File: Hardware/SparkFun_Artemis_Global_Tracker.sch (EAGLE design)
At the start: 139 parts, among them J1 IRIDIUM_9603N, J2 USB-C, J6 U.FL, J7 ANTENNA-GROUNDEDEDGE_SMA, J8 STANDOFFS_M2X0.4_STEEL_6MM, J9 STANDOFFS_M2X0.4_STEEL_6MM, Q1 5.8A/30V/35mΩ, Q2 20V/4.2A/52mΩ/1.4W, Q3 20V/4.2A/52mΩ/1.4W, Q4 600mA/40V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

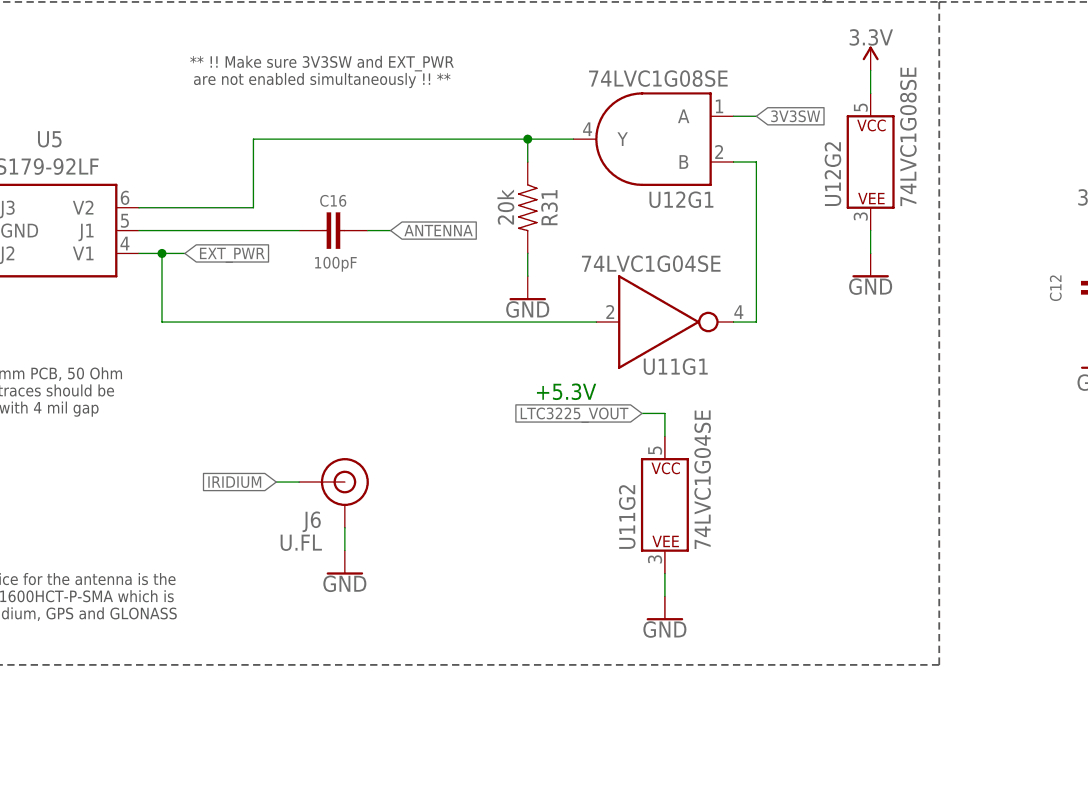
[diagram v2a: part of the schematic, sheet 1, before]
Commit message: powering U11 from 3.3V
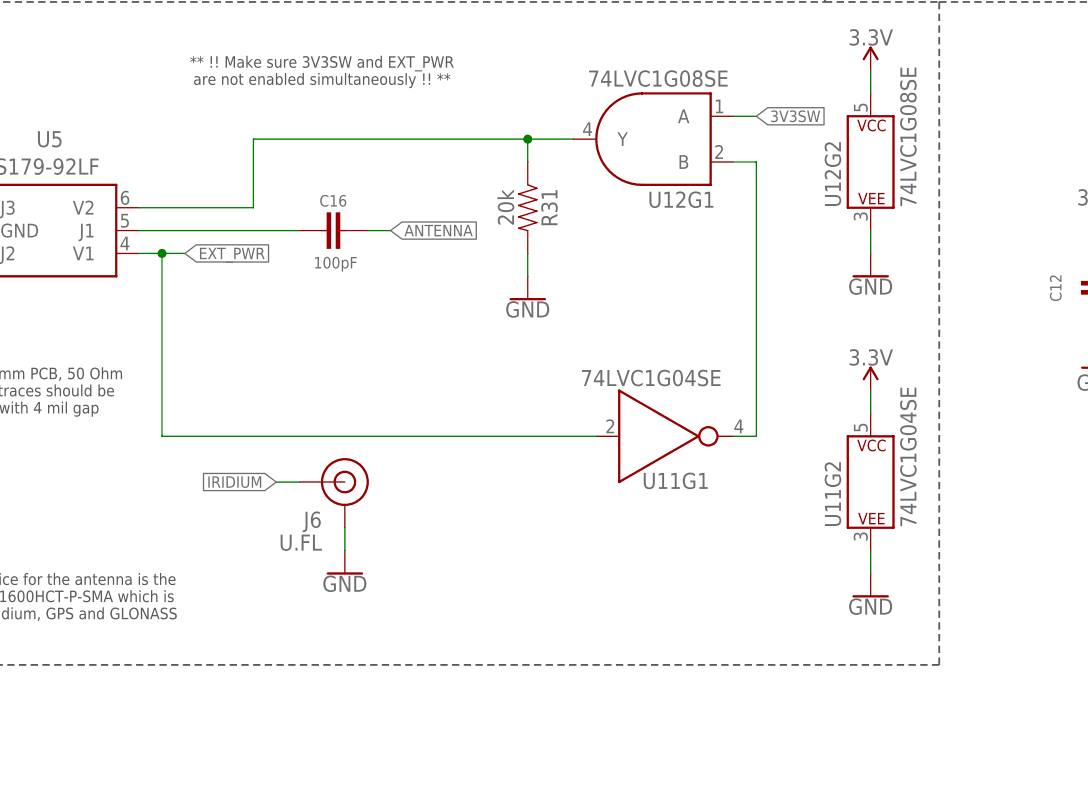
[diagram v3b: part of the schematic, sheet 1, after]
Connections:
- net 3.3V: now also U11G2.P$V+
- net LTC3225_VOUT: no longer U11G2.P$V+
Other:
- moved on the sheet: U11G1, U11G2
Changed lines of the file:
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@@
 <part name="SUPPLY3" library="SparkFun-PowerSymbols" deviceset="3.3V" device=""/>
 <part name="GND3" library="SparkFun-PowerSymbols" deviceset="GND" device=""/>
+<part name="SUPPLY19" library="SparkFun-PowerSymbols" deviceset="3.3V" device=""/>
 </parts>
 <sheets>
@@
 antenna traces should be
 32 mil with 4 mil gap </text>
-<text x="266.7" y="150.622" size="1.778" layer="91" font="vector" rot="R180">+5.3V</text>
 <wire x1="304.8" y1="193.04" x2="304.8" y2="119.38" width="0.2032" layer="97" style="longdash"/>
 <wire x1="304.8" y1="119.38" x2="162.56" y2="119.38" width="0.2032" layer="97" style="longdash"/>
@@
 <attribute name="VALUE" x="236.22" y="132.08" size="1.778" layer="96" font="vector" rot="MR0"/>
 </instance>
-<instance part="GND40" gate="1" x="274.32" y="124.46" smashed="yes">
-<attribute name="VALUE" x="274.32" y="124.206" size="1.778" layer="96" font="vector" align="top-center"/>
+<instance part="GND40" gate="1" x="297.18" y="127" smashed="yes">
+<attribute name="VALUE" x="297.18" y="126.746" size="1.778" layer="96" font="vector" align="top-center"/>
 </instance>
 <instance part="GND44" gate="1" x="297.18" y="162.56" smashed="yes">
@@
 <attribute name="VALUE" x="302.26" y="170.18" size="1.778" layer="95" font="vector" rot="R90"/>
 </instance>
-<instance part="U11" gate="G1" x="271.78" y="157.48" smashed="yes">
-<attribute name="NAME" x="271.78" y="151.638" size="1.778" layer="95" font="vector"/>
-<attribute name="VALUE" x="264.922" y="163.068" size="1.778" layer="95" font="vector"/>
-</instance>
-<instance part="U11" gate="G2" x="274.32" y="137.16" smashed="yes">
-<attribute name="NAME" x="271.018" y="132.08" size="1.778" layer="95" font="vector" rot="R90"/>
-<attribute name="VALUE" x="279.4" y="132.08" size="1.778" layer="95" font="vector" rot="R90"/>
+<instance part="U11" gate="G1" x="271.78" y="144.78" smashed="yes">
+<attribute name="NAME" x="271.78" y="138.938" size="1.778" layer="95" font="vector"/>
+<attribute name="VALUE" x="264.922" y="150.368" size="1.778" layer="95" font="vector"/>
+</instance>
+<instance part="U11" gate="G2" x="297.18" y="139.7" smashed="yes">
+<attribute name="NAME" x="293.878" y="134.62" size="1.778" layer="95" font="vector" rot="R90"/>
+<attribute name="VALUE" x="302.26" y="134.62" size="1.778" layer="95" font="vector" rot="R90"/>
 </instance>
 <instance part="R31" gate="G$1" x="259.08" y="170.18" smashed="yes" rot="R270">
@@
 <instance part="GND3" gate="1" x="322.58" y="152.4" smashed="yes">
 <attribute name="VALUE" x="320.04" y="149.86" size="1.778" layer="96" font="vector"/>
+</instance>
+<instance part="SUPPLY19" gate="G$1" x="297.18" y="149.86" smashed="yes">
+<attribute name="VALUE" x="297.18" y="152.654" size="1.778" layer="96" font="vector" align="bottom-center"/>
 </instance>
 </instances>
@@
 <pinref part="SUPPLY13" gate="G$1" pin="3.3V"/>
 <wire x1="332.74" y1="167.64" x2="332.74" y2="165.1" width="0.1524" layer="91"/>
+</segment>
+<segment>
+<pinref part="SUPPLY19" gate="G$1" pin="3.3V"/>
+<wire x1="297.18" y1="149.86" x2="297.18" y2="147.32" width="0.1524" layer="91"/>
+<pinref part="U11" gate="G2" pin="P$V+"/>
 </segment>
 </net>
@@
 </segment>
 <segment>
-<wire x1="274.32" y1="129.54" x2="274.32" y2="127" width="0.1524" layer="91"/>
+<wire x1="297.18" y1="132.08" x2="297.18" y2="129.54" width="0.1524" layer="91"/>
 <pinref part="GND40" gate="1" pin="GND"/>
 <pinref part="U11" gate="G2" pin="P$V-"/>
@@
 <wire x1="215.9" y1="165.1" x2="218.44" y2="165.1" width="0.1524" layer="91"/>
 <wire x1="218.44" y1="165.1" x2="220.98" y2="165.1" width="0.1524" layer="91"/>
-<wire x1="218.44" y1="165.1" x2="218.44" y2="157.48" width="0.1524" layer="91"/>
+<wire x1="218.44" y1="165.1" x2="218.44" y2="144.78" width="0.1524" layer="91"/>
 <junction x="218.44" y="165.1"/>
-<wire x1="218.44" y1="157.48" x2="266.7" y2="157.48" width="0.1524" layer="91"/>
+<wire x1="218.44" y1="144.78" x2="266.7" y2="144.78" width="0.1524" layer="91"/>
 <pinref part="U11" gate="G1" pin="A"/>
 </segment>
@@
 <label x="83.82" y="266.7" size="1.27" layer="95" font="vector" xref="yes"/>
 </segment>
-<segment>
-<wire x1="274.32" y1="147.32" x2="271.78" y2="147.32" width="0.1524" layer="91"/>
-<label x="271.78" y="147.32" size="1.27" layer="95" font="vector" rot="R180" xref="yes"/>
-<wire x1="274.32" y1="144.78" x2="274.32" y2="147.32" width="0.1524" layer="91"/>
-<pinref part="U11" gate="G2" pin="P$V+"/>
-</segment>
 </net>
 <net name="ARTEMIS_D28" class="0">
@@
 <net name="N$33" class="0">
 <segment>
-<wire x1="284.48" y1="157.48" x2="284.48" y2="175.26" width="0.1524" layer="91"/>
+<wire x1="284.48" y1="144.78" x2="284.48" y2="175.26" width="0.1524" layer="91"/>
 <wire x1="284.48" y1="175.26" x2="281.94" y2="175.26" width="0.1524" layer="91"/>
 <pinref part="U12" gate="G1" pin="B"/>
 <pinref part="U11" gate="G1" pin="Y"/>
-<wire x1="284.48" y1="157.48" x2="281.94" y2="157.48" width="0.1524" layer="91"/>
-</segment>
-</net>
+<wire x1="284.48" y1="144.78" x2="281.94" y2="144.78" width="0.1524" layer="91"/>
+</segment>
+</net>

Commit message: schematic tightening and moving most to first sheet
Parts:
- removed FRAME4: FRAME-LETTER, SparkFun-Aesthetics:FRAME-LETTER
- added LOGO1: SFE_LOGO_NAME.1_INCH, SparkFun-Aesthetics:SFE_LOGO_NAME.1_INCH
- added LOGO2: SFE_LOGO_NAME_FLAME.1_INCH, SparkFun-Aesthetics:SFE_LOGO_NAME_FLAME.1_INCH

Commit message: antenna switch circuit added in
-added antenna switch protection circuit.
-a few parts moved to 0402 packages to make room
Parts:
- C13, C28, C7: device SparkFun-Capacitors:0.1UF-0603-25V-(+80/-20%) -> SparkFun-Capacitors:0.1UF-0402T-16V-10%
- FRAME3: value FRAME-LETTER -> FRAME-LETTERNO_PACKAGE; device SparkFun-Aesthetics:FRAME-LETTER -> SparkFun-Aesthetics:FRAME-LETTERNO_PACKAGE; REV (none) -> v10; VERSION (none) -> v10
- FRAME5: REV (none) -> v10
- J2: device SparkFun-Connectors:USB_C_2-LAYER -> SparkFun-Connectors:USB_C_2-LAYER_PADS
- R10, R11: device SparkFun-Resistors:100OHM-0603-1/10W-1% -> SparkFun-Resistors:100OHM-0402-TIGHT-1/16W-1%
- R14, R17, R22, R23, R30, R5: value 10k -> 10K; device SparkFun-Resistors:10KOHM-0603-1/10W-1% -> SparkFun-Resistors:10KOHM-0402-1/10W-0.1%
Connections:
- net ARTEMIS_BOOT: now also U7.~BOOT(SDO5/RX1/32KHZ); no longer U7.~BOOT(MOSI5/RX1/32KHZ)
- net ARTEMIS_D10: now also U7.(SDO1/TX1/PDMCLK)D10; no longer U7.(MOSI1/TX1/PDMCLK)D10
- net ARTEMIS_D25: now also U7.(SDA2/SDI2/RX1)~D25; no longer U7.(SDA2/MISO2/RX1)~D25
- net ARTEMIS_D28: now also U7.(SDO2/I2SWCLK)~D28; no longer U7.(MOSI2/I2SWCLK)~D28
- net ARTEMIS_D40_SDA4: now also U7.(SDA4/SDI4/RX1)D40; no longer U7.(SDA4/MISO4/RX1)D40
- net ARTEMIS_D6_MISO: now also U7.(SDA0/SDI0/I2SDAT)~D6; no longer U7.(SDA0/MISO0/I2SDAT)~D6
- net ARTEMIS_D7_MOSI: now also U7.(SDO0/CLKOUT)~D7; no longer U7.(MOSI0/CLKOUT)~D7
- net ARTEMIS_D9_SDA: now also U7.(SDA1/SDI1/RX1/SCCIO)D9; no longer U7.(SDA1/MISO1/RX1/SCCIO)D9
- net ARTEMIS_RX0: now also U7.~D49(RX0/SDA5/SDI5); no longer U7.~D49(RX0/SDA5/MISO5)
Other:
- note added: "Paul Clark (Based on the SparkFun Artemis and Qwiic ZOE-M8Q)"
- note added: "Revised by: Pete Lewis"
- note removed: "Paul Clark Based on the SparkFun Artemis and Qwiic ZOE-M8Q"
- note removed: "V2"
- note removed: "v10"

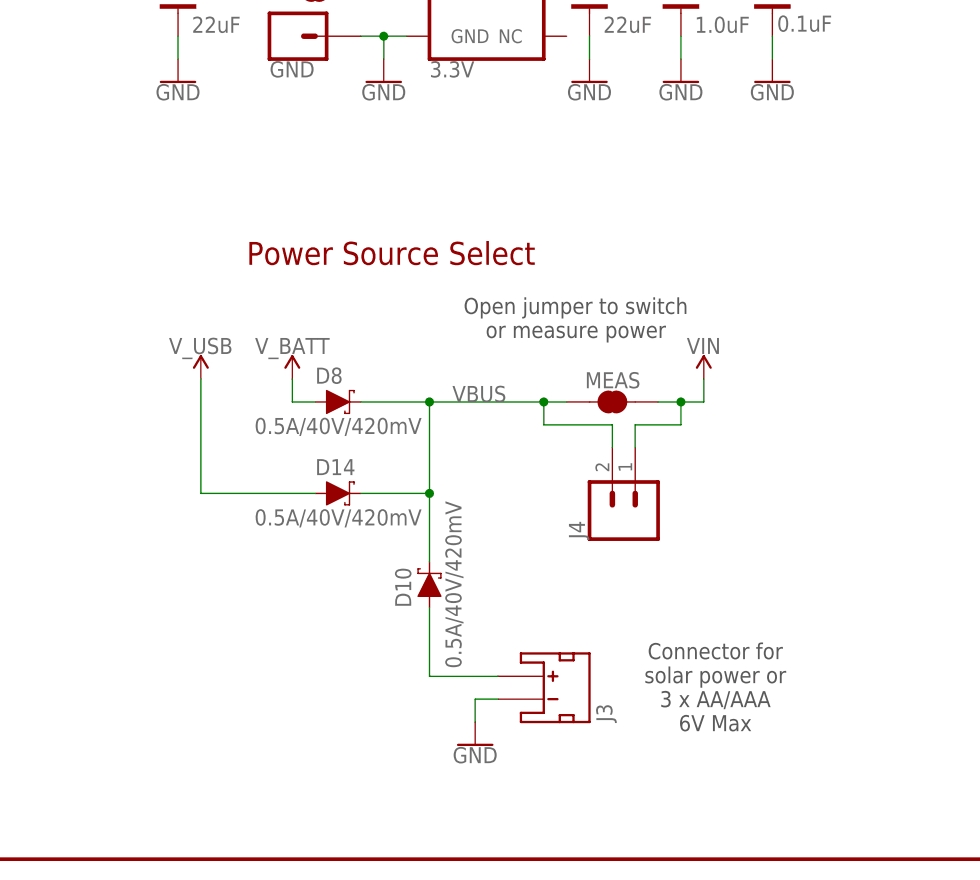
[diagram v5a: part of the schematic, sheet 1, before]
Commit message: Switched D8 to a P-CH MOSFET
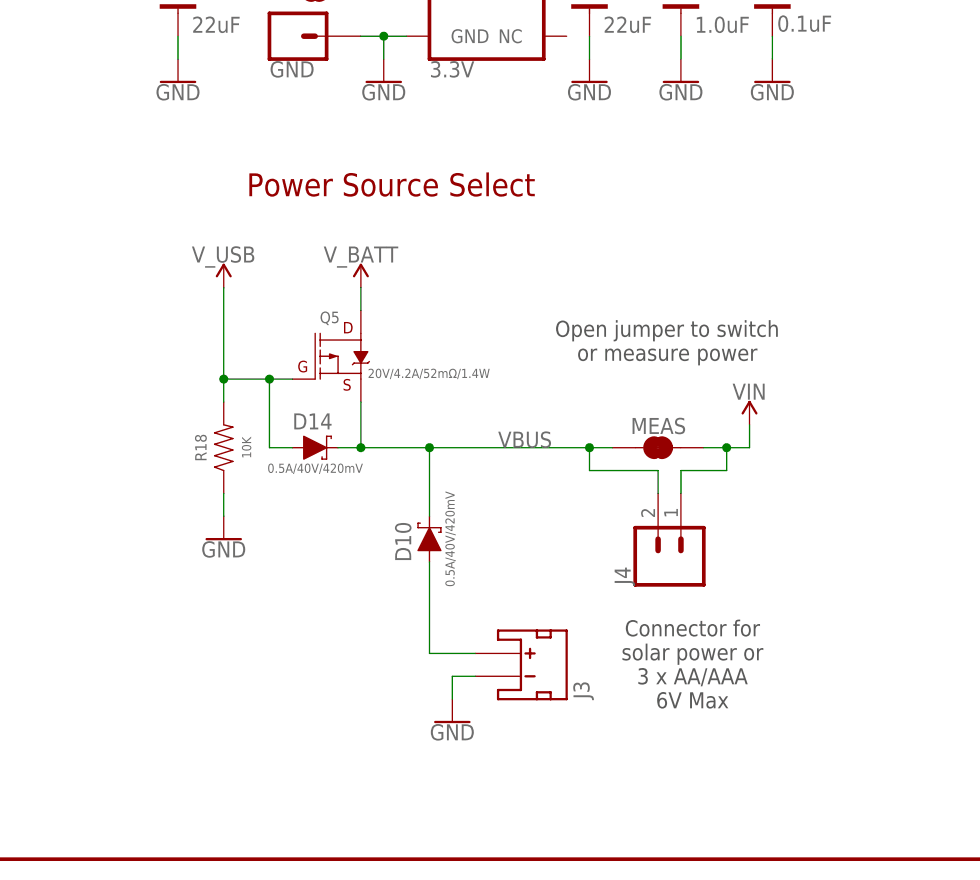
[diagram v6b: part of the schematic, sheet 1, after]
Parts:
- removed D8: 0.5A/40V/420mV, SparkFun-DiscreteSemi:DIODE-SCHOTTKY-PMEG4005EJ
- added Q5: 20V/4.2A/52mΩ/1.4W, SparkFun-DiscreteSemi:MOSFET_PCH-DMG2305UX-7
- added R18: 10K, SparkFun-Resistors:10KOHM-0402-1/10W-0.1%
- R20, R4: device SparkFun-Resistors:5.1KOHM5.1KOHM-0603-1/10W-1% -> SparkFun-Resistors:5.1KOHM-0402T-1/16W-1%
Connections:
- net GND: now also R18.1
- net VBUS: now also Q5.S; no longer D8.C
- net V_BATT: now also Q5.D; no longer D8.A
- net V_USB: now also Q5.G, R18.2
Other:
- moved on the sheet: D10, D14, J3, J4, MEAS

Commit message: schematic cleanup/tightening
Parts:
- QWIIC: value QWIIC_RIGHT_ANGLE -> QWIIC_RA
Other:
- note added: "Connections/I2C/Qwiic"
- note removed: "Connections"
- note removed: "I2C/Qwiic"
- moved on the sheet: 3V3EN, C1, C12, C17, C18, C19, C20, C21, C22, C23, C24, C25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

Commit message: silk updates almost done
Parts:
- added 3V3SW, D17, D41: TEST-POINT3X5, SparkFun-Connectors:TEST-POINT3X5
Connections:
- net 3V3SW: now also 3V3SW.1
- net ARTEMIS_D17: now also D17.1
- net ARTEMIS_D41: now also D41.1
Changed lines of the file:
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@@
 <part name="R18" library="SparkFun-Resistors" deviceset="10KOHM" device="-0402-1/10W-0.1%" value="10K"/>
 <part name="GND10" library="SparkFun-PowerSymbols" deviceset="GND" device=""/>
+<part name="3V3SW" library="SparkFun-Connectors" deviceset="TEST-POINT" device="3X5" value=""/>
+<part name="D17" library="SparkFun-Connectors" deviceset="TEST-POINT" device="3X5" value=""/>
+<part name="D41" library="SparkFun-Connectors" deviceset="TEST-POINT" device="3X5" value=""/>
 </parts>
 <sheets>
@@
 <attribute name="VALUE" x="220.98" y="83.566" size="1.778" layer="96" font="vector" align="top-center"/>
 </instance>
+<instance part="3V3SW" gate="G$1" x="149.86" y="144.78" smashed="yes">
+<attribute name="NAME" x="153.67" y="144.272" size="1.27" layer="95" font="vector"/>
+</instance>
+<instance part="D17" gate="G$1" x="236.22" y="215.9" smashed="yes">
+<attribute name="NAME" x="240.03" y="215.392" size="1.27" layer="95" font="vector"/>
+</instance>
+<instance part="D41" gate="G$1" x="236.22" y="213.36" smashed="yes">
+<attribute name="NAME" x="240.03" y="212.852" size="1.27" layer="95" font="vector"/>
+</instance>
 </instances>
 <busses>
@@
 <wire x1="215.9" y1="254" x2="208.28" y2="254" width="0.1524" layer="91"/>
 <label x="208.28" y="254" size="1.27" layer="95" font="vector" rot="R180" xref="yes"/>
+</segment>
+<segment>
+<label x="233.68" y="215.9" size="1.27" layer="95" font="vector" rot="R180" xref="yes"/>
+<pinref part="D17" gate="G$1" pin="1"/>
+<wire x1="233.68" y1="215.9" x2="236.22" y2="215.9" width="0.1524" layer="91" style="longdash"/>
 </segment>
 </net>
@@
 <wire x1="147.32" y1="149.86" x2="149.86" y2="149.86" width="0.1524" layer="91"/>
 <label x="149.86" y="149.86" size="1.27" layer="95" font="vector" xref="yes"/>
+<wire x1="147.32" y1="149.86" x2="147.32" y2="144.78" width="0.1524" layer="91" style="longdash"/>
+<junction x="147.32" y="149.86"/>
+<pinref part="3V3SW" gate="G$1" pin="1"/>
+<wire x1="147.32" y1="144.78" x2="149.86" y2="144.78" width="0.1524" layer="91" style="longdash"/>
 </segment>
 <segment>
@@
 <label x="261.62" y="246.38" size="1.27" layer="95" font="vector" xref="yes"/>
 </segment>
-</net>
+<segment>
+<wire x1="236.22" y1="213.36" x2="233.68" y2="213.36" width="0.1524" layer="91"/>
+<label x="233.68" y="213.36" size="1.27" layer="95" font="vector" rot="R180" xref="yes"/>
+<pinref part="D41" gate="G$1" pin="1"/>
+</segment>
+</net>
